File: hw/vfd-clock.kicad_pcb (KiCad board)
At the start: 2 copper layers, 150 x 50 mm, 45 parts, among them CON1 BARREL_JACK_2, CON2 BARREL_JACK_2, P1 ST_LINK, P2 GPS, Q1 PNP, Q2 PNP, SW1 SET, SW2 UP, SW3 DOWN, SW4 DIM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

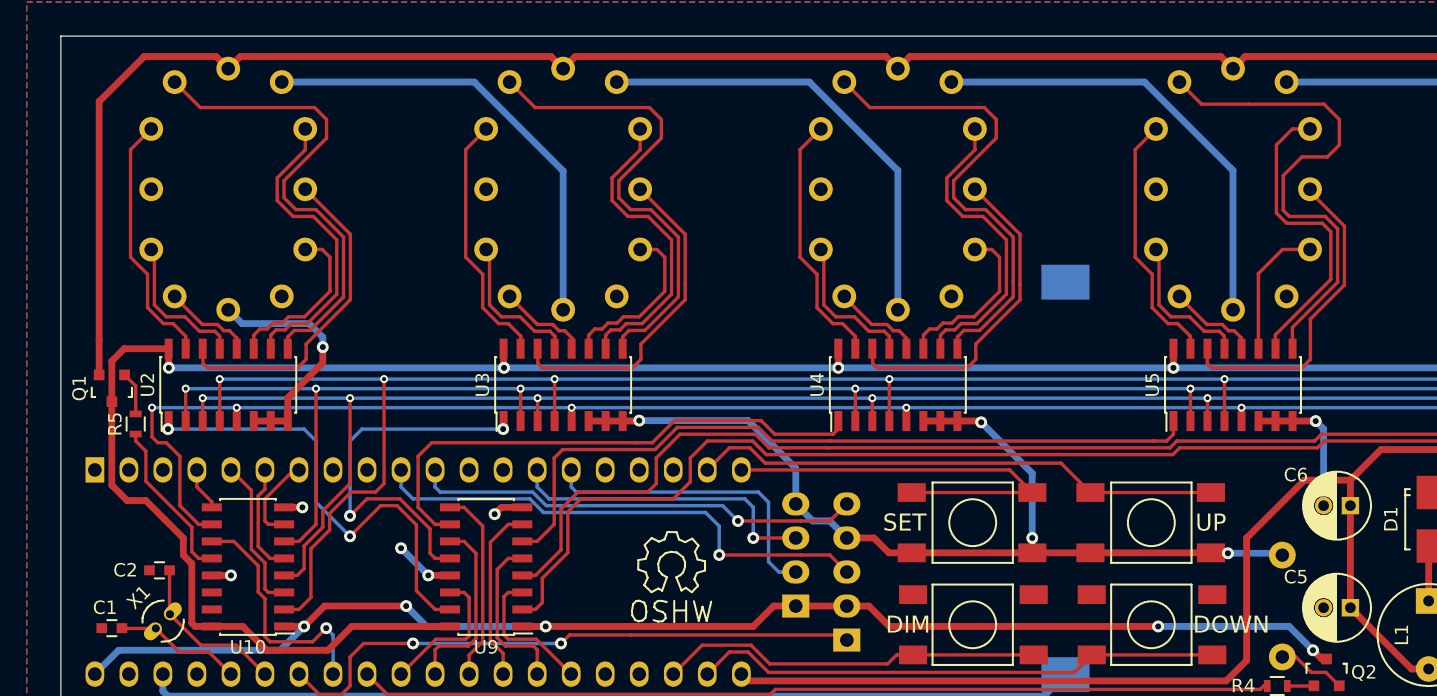
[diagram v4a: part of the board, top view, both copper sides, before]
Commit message: last level shifter output lights decimal points
specifically the 2nd and 4th, i.e. between the hours/minutes and
minutes/seconds
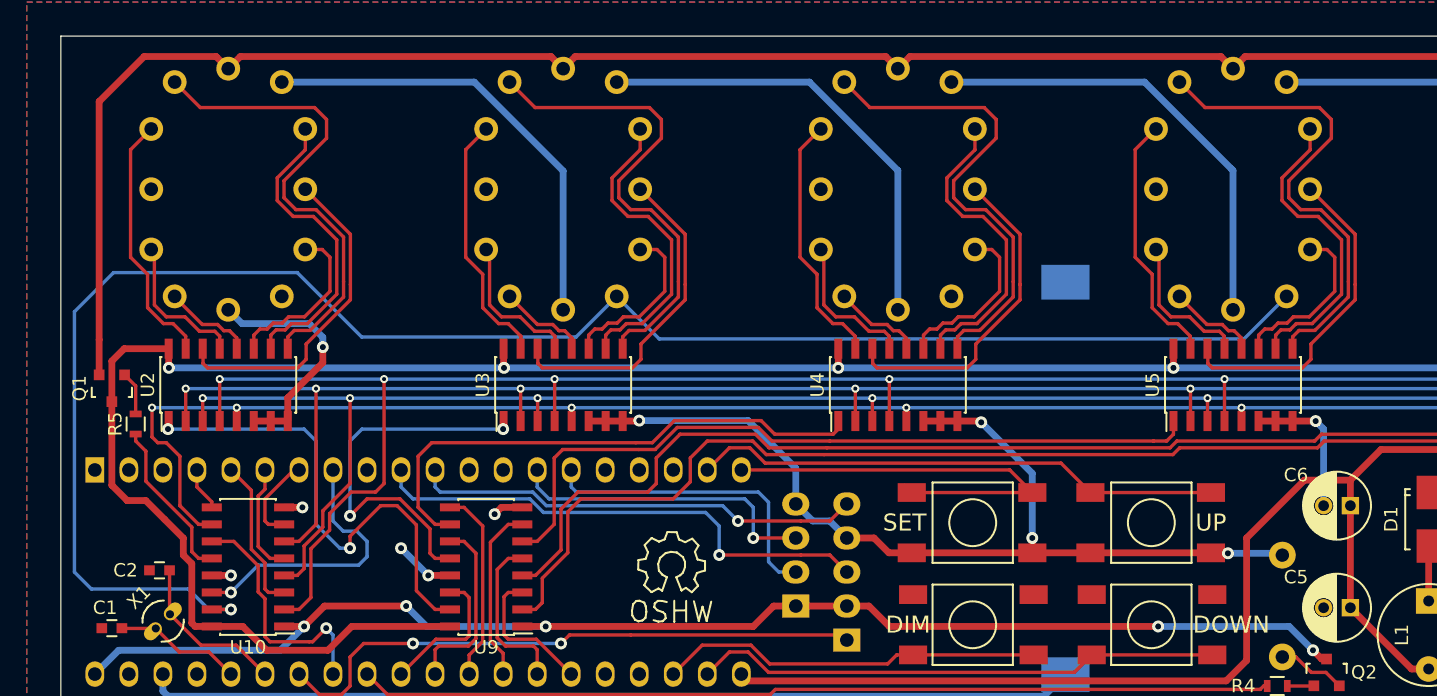
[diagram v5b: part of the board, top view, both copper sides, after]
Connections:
- U1 pad 8: (no net) -> /DPL
- U10 pad 14: (no net) -> /DPL
- U10 pad 15: (no net) -> /DPH
- V2 pad 5: (no net) -> /DPH
- V4 pad 5: (no net) -> /DPH
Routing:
- net /DPH: track 0.00 -> 131.3 mm, vias 0 -> 1
- net /DPL: track 0.00 -> 20.8 mm, vias 0 -> 1
- net /C4: track 10.2 -> 12.7 mm
- net /STROBE1H: track 34.7 -> 36.9 mm
- net /A4: track 37.7 -> 36.1 mm
- net /G4: track 24.0 -> 24.8 mm

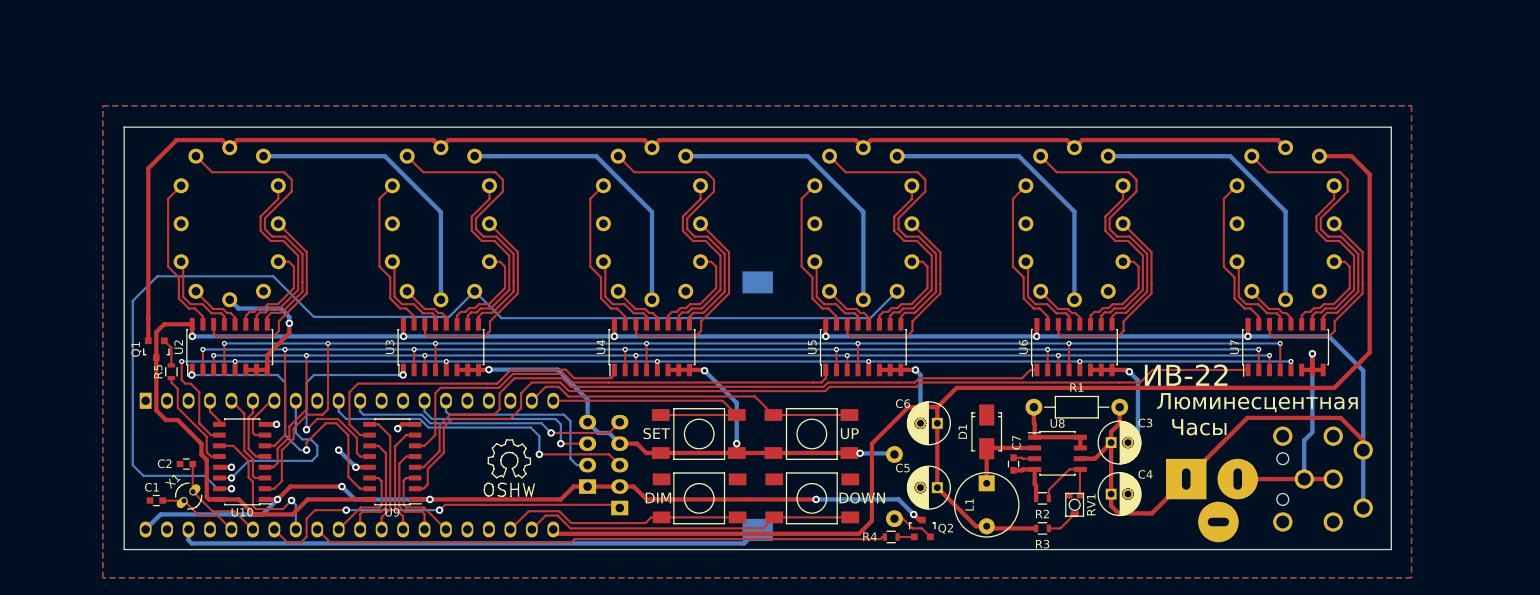
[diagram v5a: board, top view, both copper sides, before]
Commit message: mount holes, tweaks to ground fill, gerbers
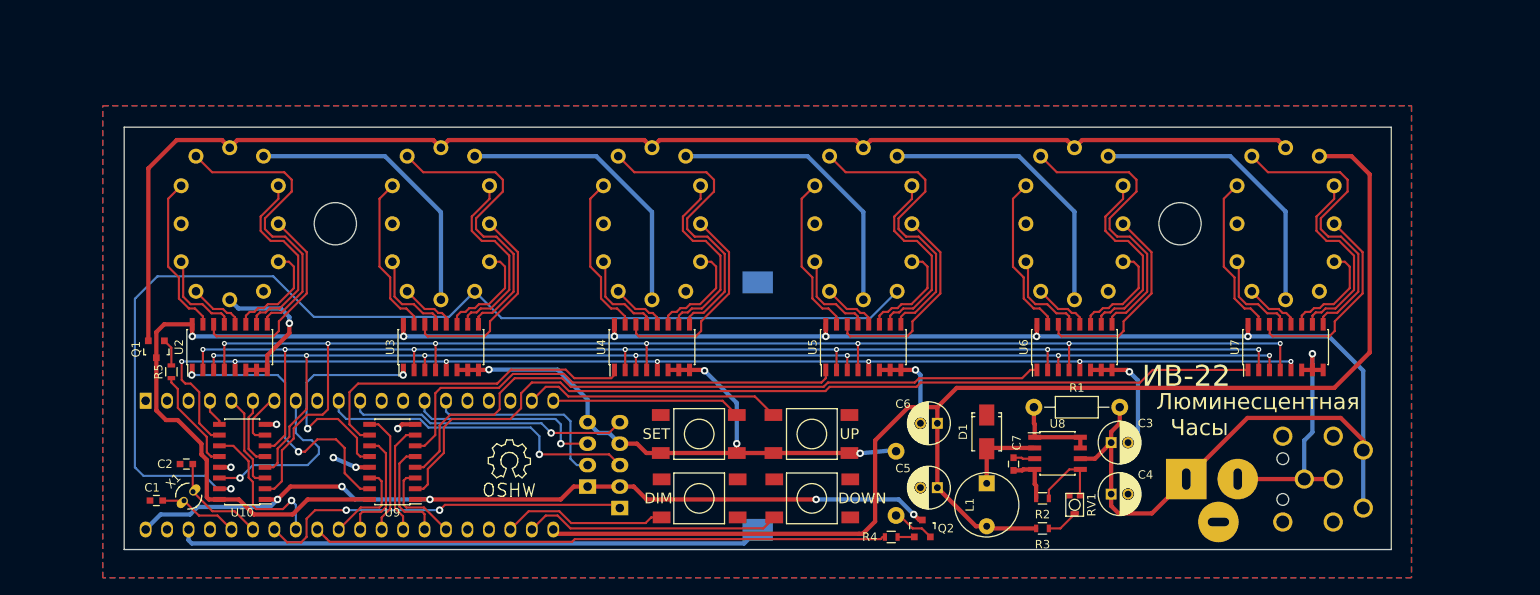
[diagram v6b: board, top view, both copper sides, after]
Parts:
- added M1: MountingHole_4-5mm, Mounting_Holes:MountingHole_5mm, F.Cu at (50.4, 36.8)
- added M2: MountingHole_4-5mm, Mounting_Holes:MountingHole_5mm, F.Cu at (150.4, 36.8)
- moved SP1 0.43 mm to (116.8, 67.6)
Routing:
- net /BTN_SET: track 32.2 -> 23.2 mm
- net /BTN_UP: track 39.7 -> 30.7 mm
- net /BTN_DIM: track 28.7 -> 19.7 mm
- net /BTN_DN: track 39.6 -> 30.6 mm
- net /STROBE1H: track 36.9 -> 34.1 mm

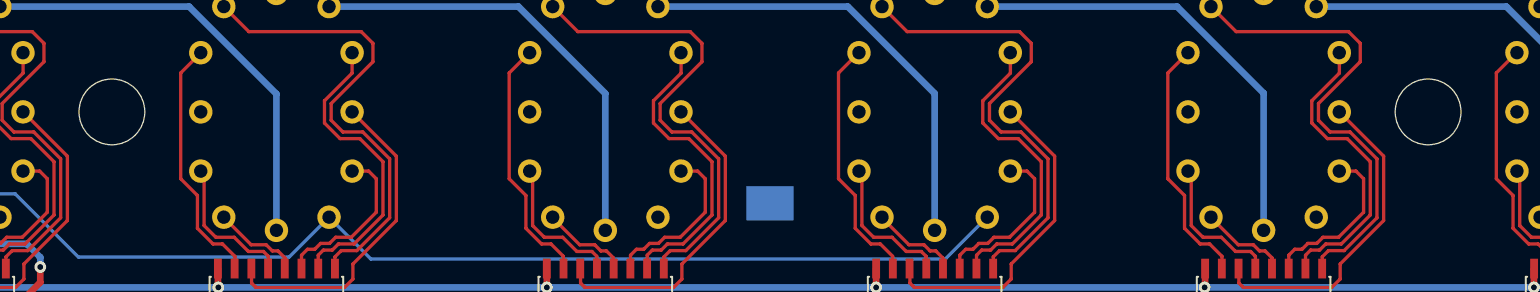
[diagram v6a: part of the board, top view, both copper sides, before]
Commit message: move mount holes to work well with plastic stand
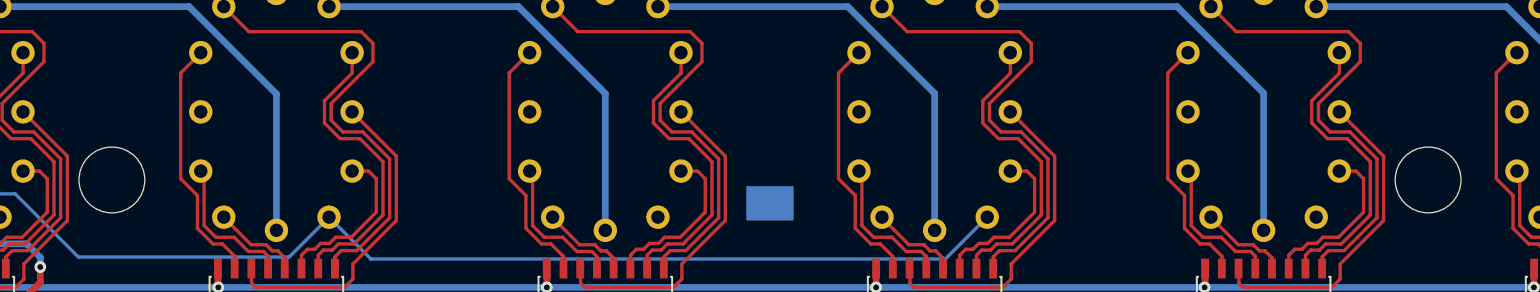
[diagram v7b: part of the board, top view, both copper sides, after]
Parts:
- moved M1 5.17 mm to (50.4, 42.0)
- moved M2 5.17 mm to (150.4, 42.0)

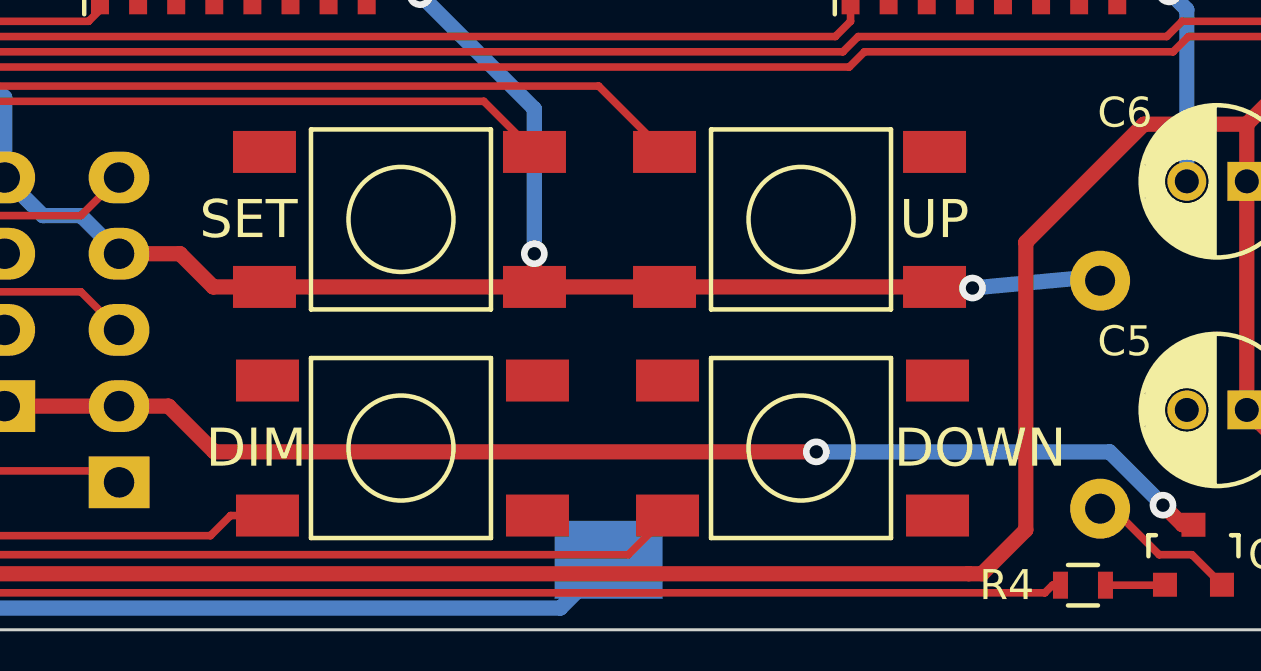
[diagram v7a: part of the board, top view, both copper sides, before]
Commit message: fix missing silksreen text
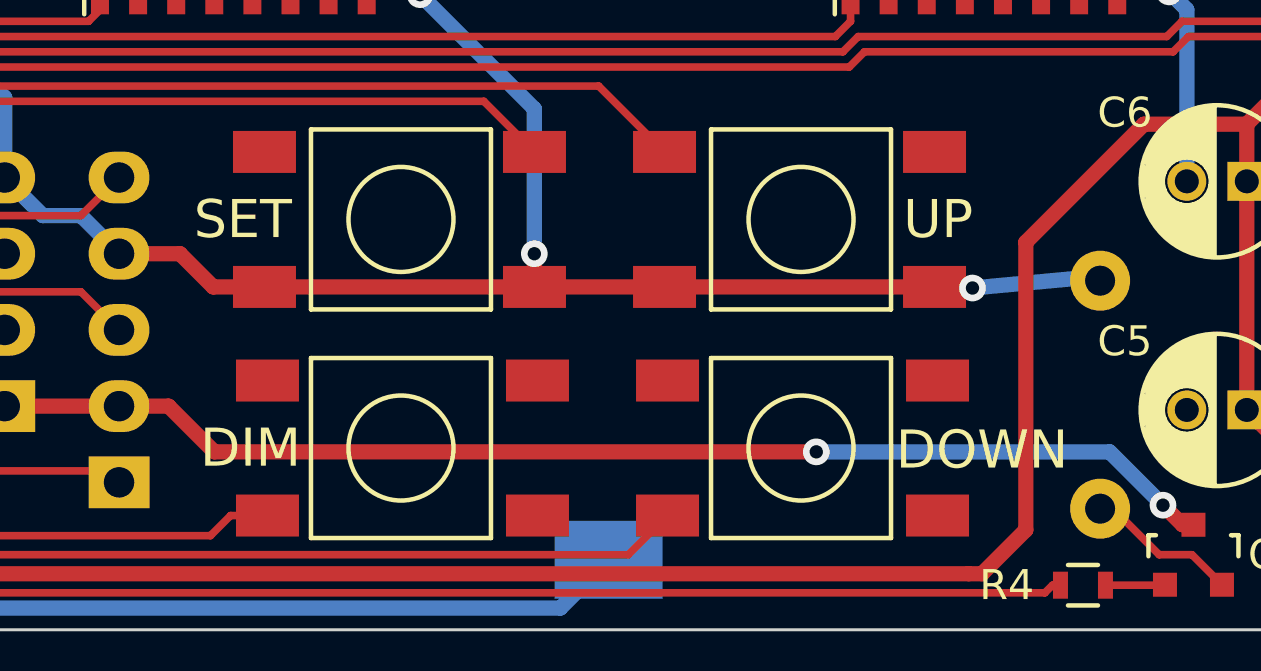
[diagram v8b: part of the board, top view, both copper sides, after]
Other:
- board text added: "DIM"
- board text added: "DOWN"
- board text added: "SET"
- board text added: "UP"
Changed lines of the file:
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@@
     (area 22.86 19.95297 177.800001 78.740001)
     (thickness 1.6)
-    (drawings 7)
+    (drawings 11)
     (tracks 1042)
     (zones 0)
@@
       (effects (font (size 1 1) (thickness 0.15)))
     )
-    (fp_text value SET (at -5.08 0) (layer F.SilkS)
+    (fp_text value SET (at -5.2705 0) (layer F.SilkS) hide
       (effects (font (size 1.27 1.27) (thickness 0.15)))
     )
@@
       (effects (font (size 1 1) (thickness 0.15)))
     )
-    (fp_text value UP (at 4.445 0) (layer F.SilkS)
+    (fp_text value UP (at 4.445 0) (layer F.SilkS) hide
       (effects (font (size 1.27 1.27) (thickness 0.15)))
     )
@@
       (effects (font (size 1 1) (thickness 0.15)))
     )
-    (fp_text value DOWN (at -5.969 0 180) (layer F.SilkS)
+    (fp_text value DOWN (at -5.969 0 180) (layer F.SilkS) hide
       (effects (font (size 1.27 1.27) (thickness 0.15)))
     )
@@
       (effects (font (size 1 1) (thickness 0.15)))
     )
-    (fp_text value DIM (at 4.826 0 180) (layer F.SilkS)
+    (fp_text value DIM (at 5.0165 0 180) (layer F.SilkS) hide
       (effects (font (size 1.27 1.27) (thickness 0.15)))
     )
@@
     (pad 1 thru_hole circle (at 0 0) (size 5 5) (drill 5) (layers))
   )
+  (gr_text DIM (at 88.4555 69.342) (layer F.SilkS)
+    (effects (font (size 1.27 1.27) (thickness 0.15)))
+  )
+  (gr_text SET (at 88.2015 61.722) (layer F.SilkS)
+    (effects (font (size 1.27 1.27) (thickness 0.15)))
+  )
+  (gr_text DOWN (at 112.8395 69.4055) (layer F.SilkS)
+    (effects (font (size 1.27 1.27) (thickness 0.15)))
+  )
+  (gr_text UP (at 111.379 61.722) (layer F.SilkS)
+    (effects (font (size 1.27 1.27) (thickness 0.15)))
+  )
   (gr_text "SWDIO\nGND\nSWCLK\n3v3\nRST" (at 85.598 65.405) (layer B.SilkS)
